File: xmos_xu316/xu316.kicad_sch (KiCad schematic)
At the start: 18 parts, among them J1 Conn_02x14_Odd_Even, J2 Conn_02x14_Odd_Even, J3 USB_C_Receptacle_USB2.0_16P, U1 XU316-1024-QF60B-C24, U2 USB6B1, U3 W25Q128JVS, Y1 Crystal_GND24

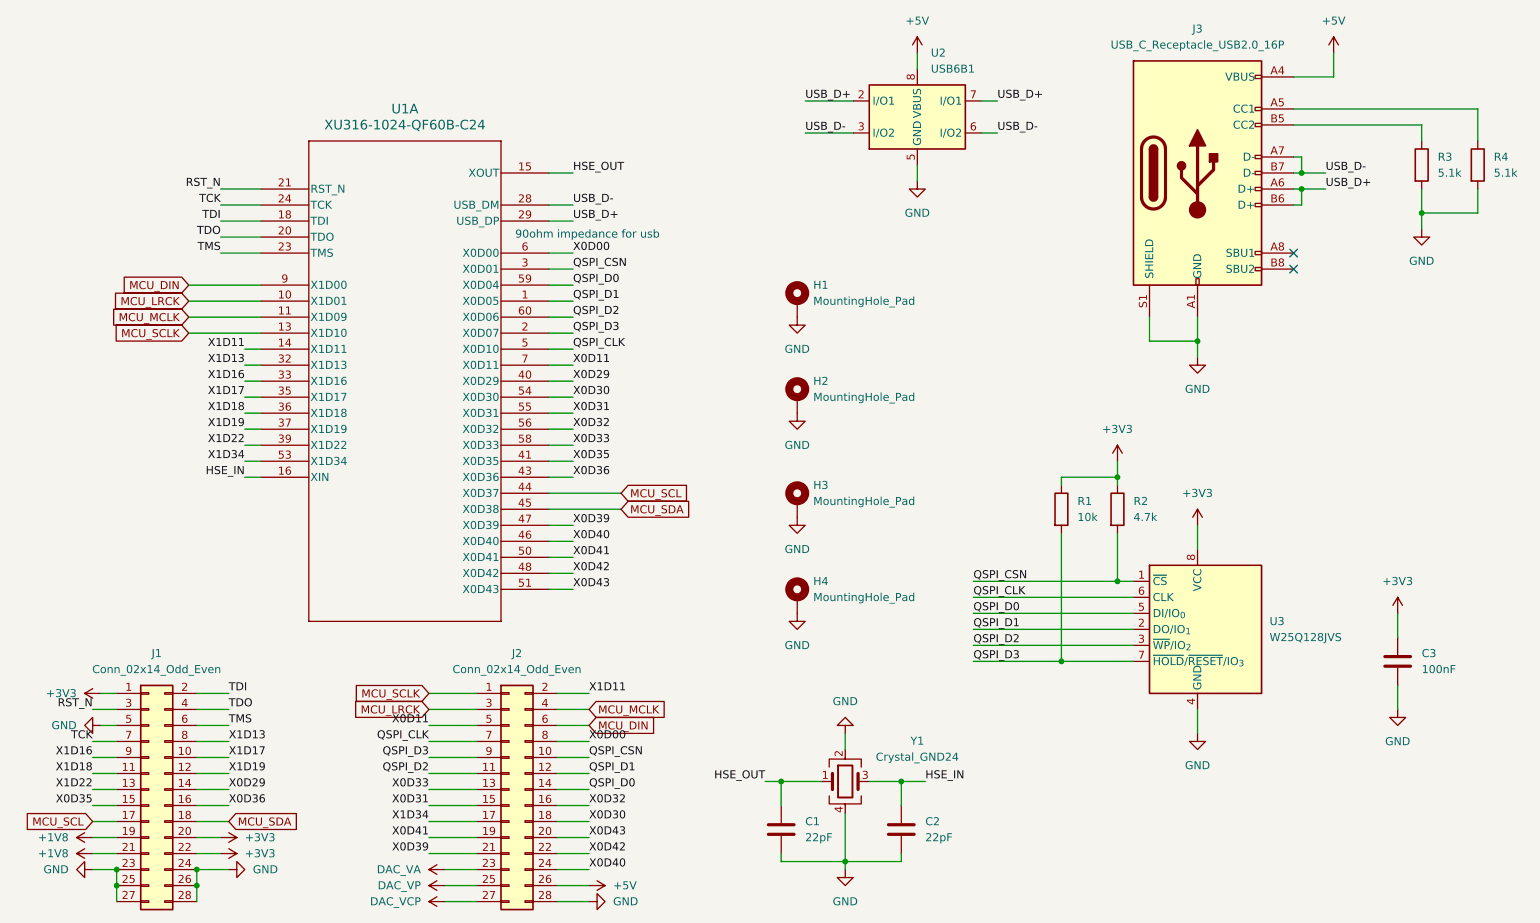
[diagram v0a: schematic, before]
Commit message: fixed pcb errors
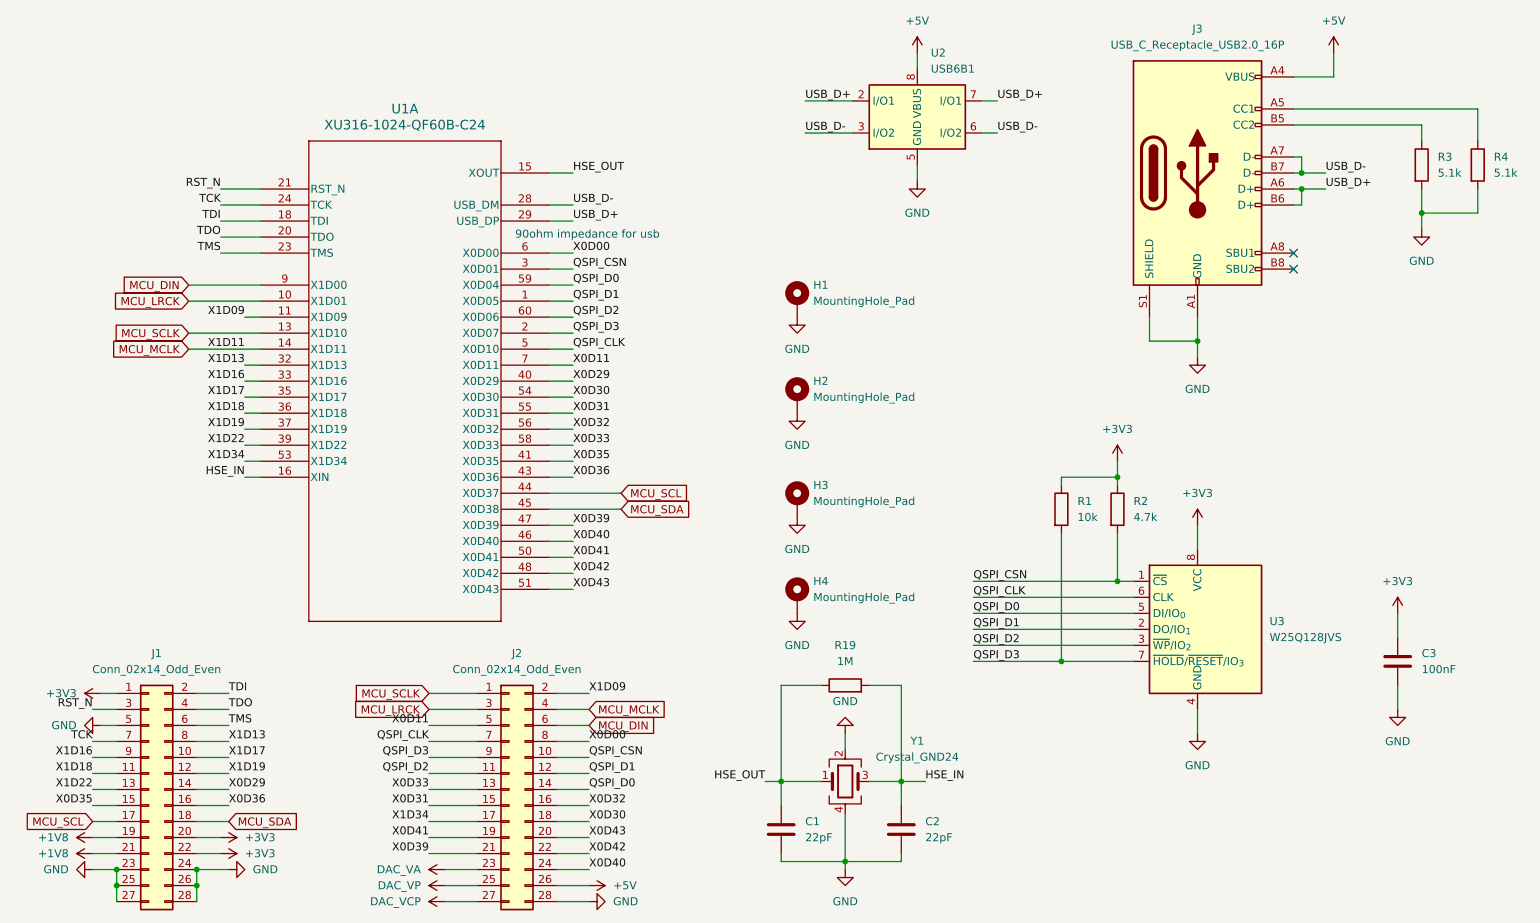
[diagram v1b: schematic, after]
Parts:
- added R19: 1M, Resistor_SMD:R_0603_1608Metric, symbol Device:R
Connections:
- net HSE_IN: now also R19.2
- net HSE_OUT: now also R19.1
- net MCU_MCLK: now also U1.14 (X1D11); no longer U1.11 (X1D09)
- net X1D11 renamed X1D09
- net X1D09: now also U1.11 (X1D09); no longer U1.14 (X1D11)
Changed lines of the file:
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@@
 	(wire
 		(pts
+			(xy 166.37 139.7) (xy 166.37 154.94)
+		)
+		(stroke
+			(width 0)
+			(type default)
+		)
+	)
+	(wire
+		(pts
 			(xy 147.32 154.94) (xy 147.32 158.75)
 		)
@@
 	(wire
 		(pts
+			(xy 53.34 86.36) (xy 64.77 86.36)
+		)
+		(stroke
+			(width 0)
+			(type default)
+		)
+	)
+	(wire
+		(pts
 			(xy 59.69 153.67) (xy 54.61 153.67)
 		)
@@
 	(wire
 		(pts
-			(xy 62.23 86.36) (xy 64.77 86.36)
-		)
-		(stroke
-			(width 0)
-			(type default)
-		)
-	)
-	(wire
-		(pts
 			(xy 191.77 115.57) (xy 191.77 135.89)
 		)
@@
 	(wire
 		(pts
-			(xy 53.34 81.28) (xy 64.77 81.28)
+			(xy 114.3 81.28) (xy 110.49 81.28)
 		)
 		(stroke
@@
 	(wire
 		(pts
-			(xy 114.3 81.28) (xy 110.49 81.28)
+			(xy 91.44 166.37) (xy 99.06 166.37)
 		)
 		(stroke
@@
 	(wire
 		(pts
-			(xy 91.44 166.37) (xy 99.06 166.37)
+			(xy 116.84 168.91) (xy 111.76 168.91)
 		)
 		(stroke
@@
 	(wire
 		(pts
-			(xy 116.84 168.91) (xy 111.76 168.91)
+			(xy 93.98 168.91) (xy 99.06 168.91)
 		)
 		(stroke
@@
 	(wire
 		(pts
-			(xy 93.98 168.91) (xy 99.06 168.91)
+			(xy 114.3 114.3) (xy 110.49 114.3)
 		)
 		(stroke
@@
 	(wire
 		(pts
-			(xy 114.3 114.3) (xy 110.49 114.3)
+			(xy 93.98 171.45) (xy 99.06 171.45)
 		)
 		(stroke
@@
 	(wire
 		(pts
-			(xy 93.98 171.45) (xy 99.06 171.45)
+			(xy 213.36 143.51) (xy 213.36 147.32)
 		)
 		(stroke
@@
 	(wire
 		(pts
-			(xy 213.36 143.51) (xy 213.36 147.32)
+			(xy 147.32 139.7) (xy 147.32 154.94)
 		)
 		(stroke
@@
 	(wire
 		(pts
+			(xy 62.23 81.28) (xy 64.77 81.28)
+		)
+		(stroke
+			(width 0)
+			(type default)
+		)
+	)
+	(wire
+		(pts
 			(xy 147.32 154.94) (xy 153.67 154.94)
 		)
@@
 	(wire
 		(pts
+			(xy 153.67 139.7) (xy 147.32 139.7)
+		)
+		(stroke
+			(width 0)
+			(type default)
+		)
+	)
+	(wire
+		(pts
 			(xy 121.92 111.76) (xy 110.49 111.76)
 		)
@@
 	(wire
 		(pts
+			(xy 161.29 139.7) (xy 166.37 139.7)
+		)
+		(stroke
+			(width 0)
+			(type default)
+		)
+	)
+	(wire
+		(pts
 			(xy 53.34 78.74) (xy 64.77 78.74)
 		)
@@
 		)
 	)
-	(label "X1D11"
+	(label "X1D09"
 		(at 116.84 140.97 0)
 		(effects
@@
 		)
 	)
+	(label "X1D09"
+		(at 62.23 81.28 180)
+		(effects
+			(font
+				(size 1.27 1.27)
+			)
+			(justify right bottom)
+		)
+	)
 	(global_label "MCU_SCLK"
 		(shape input)
@@
 	(global_label "MCU_MCLK"
 		(shape input)
-		(at 53.34 81.28 180)
+		(at 53.34 86.36 180)
 		(fields_autoplaced yes)
 		(effects
@@
 		)
 		(property "Intersheetrefs" "${INTERSHEET_REFS}"
-			(at 40.3158 81.28 0)
+			(at 40.3158 86.36 0)
 			(effects
 				(font
@@
 					(unit 1)
 				)
+			)
+		)
+	)
+	(symbol
+		(lib_id "Device:R")
+		(at 157.48 139.7 90)
+		(unit 1)
+		(exclude_from_sim no)
+		(in_bom yes)
+		(on_board yes)
+		(dnp no)
+		(fields_autoplaced yes)
+		(property "Reference" "R19"
+			(at 157.48 133.35 90)
+			(effects
+				(font
+					(size 1.27 1.27)
+				)
+			)
+		)
+		(property "Value" "1M"
+			(at 157.48 135.89 90)
+			(effects
+				(font
+					(size 1.27 1.27)
+				)
+			)
+		)
+		(property "Footprint" "Resistor_SMD:R_0603_1608Metric"
+			(at 157.48 141.478 90)
+			(effects
+				(font
+					(size 1.27 1.27)
+				)
+				(hide yes)
+			)
+		)
+		(property "Datasheet" "~"
+			(at 157.48 139.7 0)
+			(effects
+				(font
+					(size 1.27 1.27)
+				)
+				(hide yes)
+			)
+		)
+		(property "Description" "Resistor"
+			(at 157.48 139.7 0)
+			(effects
+				(font
+					(size 1.27 1.27)
+				)
+				(hide yes)
+			)
+		)
+		(pin "2"
+		)
+		(pin "1"
+		)
+		(instances
+			(project "xmos_xu316"
+				(path "/56822943-77db-41a4-96a3-a10f88783b02/f602d29d-5b8b-476b-882c-2cadecf89fa6"
+					(reference "R19")
+					(unit 1)
+				)

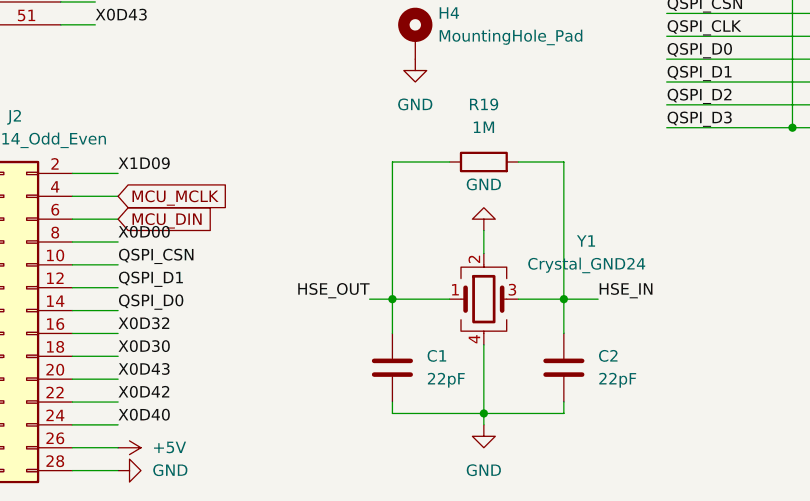
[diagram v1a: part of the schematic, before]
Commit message: add rd for HSE
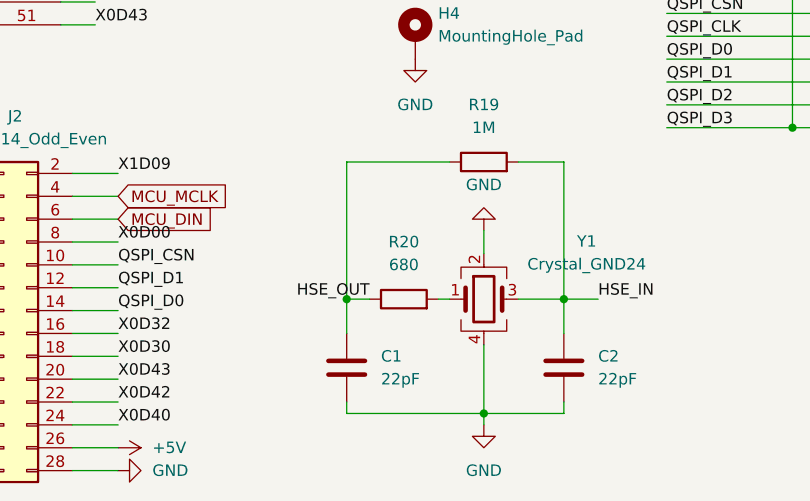
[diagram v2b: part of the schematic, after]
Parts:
- added R20: 680, Resistor_SMD:R_0603_1608Metric, symbol Device:R
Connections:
- net HSE_OUT: now also R20.1; no longer Y1.1
- new net: R20.2, Y1.1
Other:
- moved on the sheet: C1
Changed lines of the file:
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@@
 	)
 	(junction
-		(at 147.32 154.94)
+		(at 142.24 154.94)
 		(diameter 0)
 		(color 0 0 0 0)
@@
 	(wire
 		(pts
-			(xy 166.37 139.7) (xy 166.37 154.94)
+			(xy 142.24 154.94) (xy 142.24 158.75)
 		)
 		(stroke
@@
 	(wire
 		(pts
-			(xy 147.32 154.94) (xy 147.32 158.75)
+			(xy 166.37 139.7) (xy 166.37 154.94)
 		)
 		(stroke
@@
 	(wire
 		(pts
+			(xy 142.24 154.94) (xy 144.78 154.94)
+		)
+		(stroke
+			(width 0)
+			(type default)
+		)
+	)
+	(wire
+		(pts
 			(xy 166.37 154.94) (xy 161.29 154.94)
 		)
@@
 	(wire
 		(pts
+			(xy 152.4 154.94) (xy 153.67 154.94)
+		)
+		(stroke
+			(width 0)
+			(type default)
+		)
+	)
+	(wire
+		(pts
 			(xy 116.84 171.45) (xy 111.76 171.45)
 		)
@@
 	(wire
 		(pts
-			(xy 147.32 166.37) (xy 147.32 167.64)
+			(xy 142.24 166.37) (xy 142.24 167.64)
 		)
 		(stroke
@@
 	(wire
 		(pts
-			(xy 147.32 139.7) (xy 147.32 154.94)
+			(xy 142.24 139.7) (xy 142.24 154.94)
 		)
 		(stroke
@@
 	(wire
 		(pts
-			(xy 147.32 154.94) (xy 153.67 154.94)
-		)
-		(stroke
-			(width 0)
-			(type default)
-		)
-	)
-	(wire
-		(pts
 			(xy 114.3 91.44) (xy 110.49 91.44)
 		)
@@
 	(wire
 		(pts
-			(xy 147.32 167.64) (xy 157.48 167.64)
+			(xy 142.24 167.64) (xy 157.48 167.64)
 		)
 		(stroke
@@
 	(wire
 		(pts
-			(xy 153.67 139.7) (xy 147.32 139.7)
+			(xy 153.67 139.7) (xy 142.24 139.7)
 		)
 		(stroke
@@
 	(wire
 		(pts
-			(xy 144.78 154.94) (xy 147.32 154.94)
-		)
-		(stroke
-			(width 0)
-			(type default)
-		)
-	)
-	(wire
-		(pts
 			(xy 181.61 52.07) (xy 179.07 52.07)
 		)
@@
 	(symbol
 		(lib_id "Device:C")
-		(at 147.32 162.56 0)
+		(at 142.24 162.56 0)
 		(unit 1)
 		(exclude_from_sim no)
@@
 		(fields_autoplaced yes)
 		(property "Reference" "C1"
-			(at 151.13 161.2899 0)
+			(at 146.05 161.2899 0)
 			(effects
 				(font
@@
 		)
 		(property "Value" "22pF"
-			(at 151.13 163.8299 0)
+			(at 146.05 163.8299 0)
 			(effects
 				(font
@@
 		)
 		(property "Footprint" "Capacitor_SMD:C_0603_1608Metric"
-			(at 148.2852 166.37 0)
+			(at 143.2052 166.37 0)
 			(effects
 				(font
@@
 		)
 		(property "Datasheet" "~"
-			(at 147.32 162.56 0)
+			(at 142.24 162.56 0)
 			(effects
 				(font
@@
 		)
 		(property "Description" "Unpolarized capacitor"
-			(at 147.32 162.56 0)
+			(at 142.24 162.56 0)
 			(effects
 				(font
@@
 					(unit 1)
 				)
+			)
+		)
+	)
+	(symbol
+		(lib_id "Device:R")
+		(at 148.59 154.94 90)
+		(unit 1)
+		(exclude_from_sim no)
+		(in_bom yes)
+		(on_board yes)
+		(dnp no)
+		(fields_autoplaced yes)
+		(property "Reference" "R20"
+			(at 148.59 148.59 90)
+			(effects
+				(font
+					(size 1.27 1.27)
+				)
+			)
+		)
+		(property "Value" "680"
+			(at 148.59 151.13 90)
+			(effects
+				(font
+					(size 1.27 1.27)
+				)
+			)
+		)
+		(property "Footprint" "Resistor_SMD:R_0603_1608Metric"
+			(at 148.59 156.718 90)
+			(effects
+				(font
+					(size 1.27 1.27)
+				)
+				(hide yes)
+			)
+		)
+		(property "Datasheet" "~"
+			(at 148.59 154.94 0)
+			(effects
+				(font
+					(size 1.27 1.27)
+				)
+				(hide yes)
+			)
+		)
+		(property "Description" "Resistor"
+			(at 148.59 154.94 0)
+			(effects
+				(font
+					(size 1.27 1.27)
+				)
+				(hide yes)
+			)
+		)
+		(pin "2"
+		)
+		(pin "1"
+		)
+		(instances
+			(project "xmos_xu316"
+				(path "/56822943-77db-41a4-96a3-a10f88783b02/f602d29d-5b8b-476b-882c-2cadecf89fa6"
+					(reference "R20")
+					(unit 1)
+				)
